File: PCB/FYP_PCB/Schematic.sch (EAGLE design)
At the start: 14 parts, among them IC1 7805TV

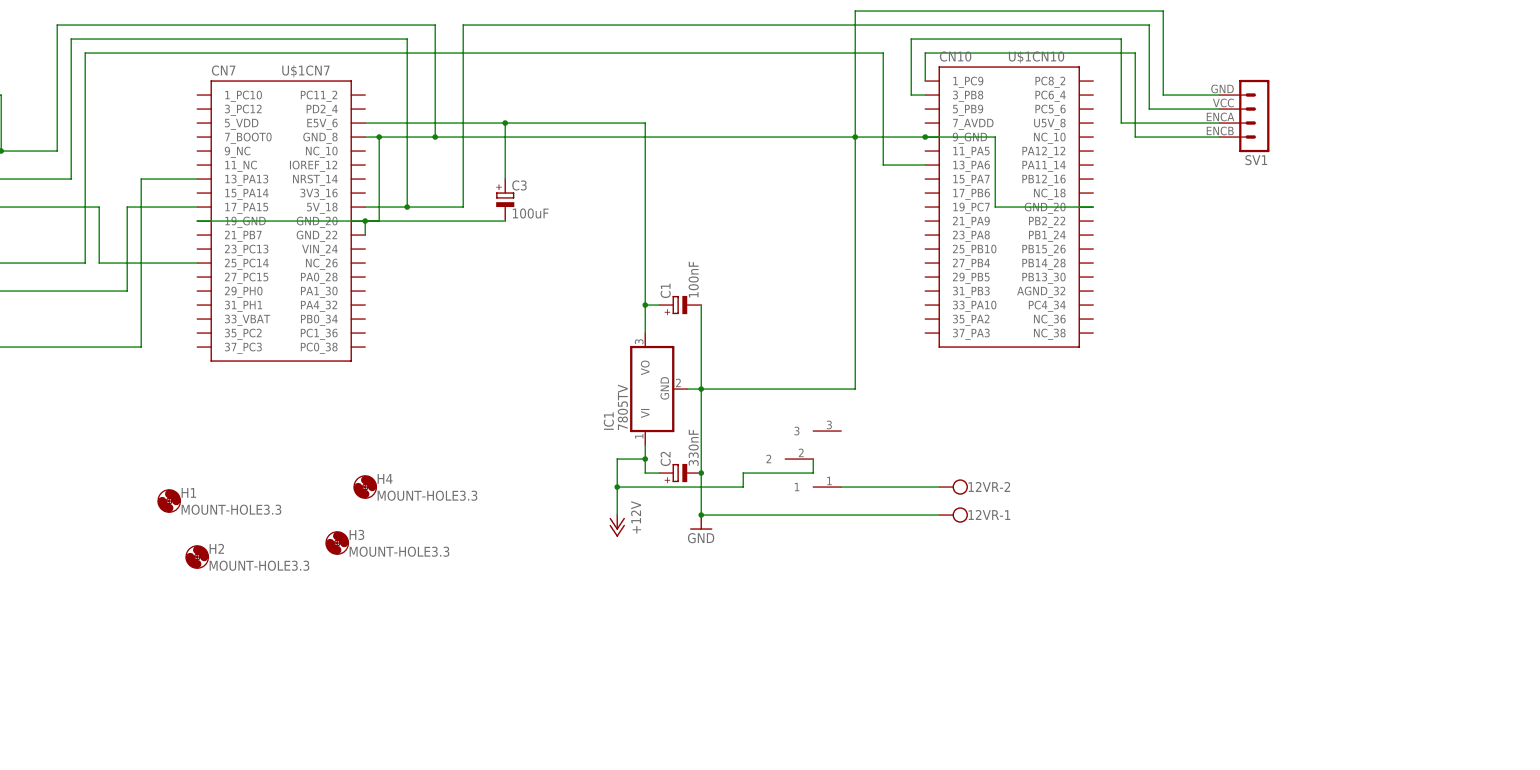
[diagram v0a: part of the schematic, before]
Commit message: Update PCB for new pin configurations. Add HC05 bluetooth module.
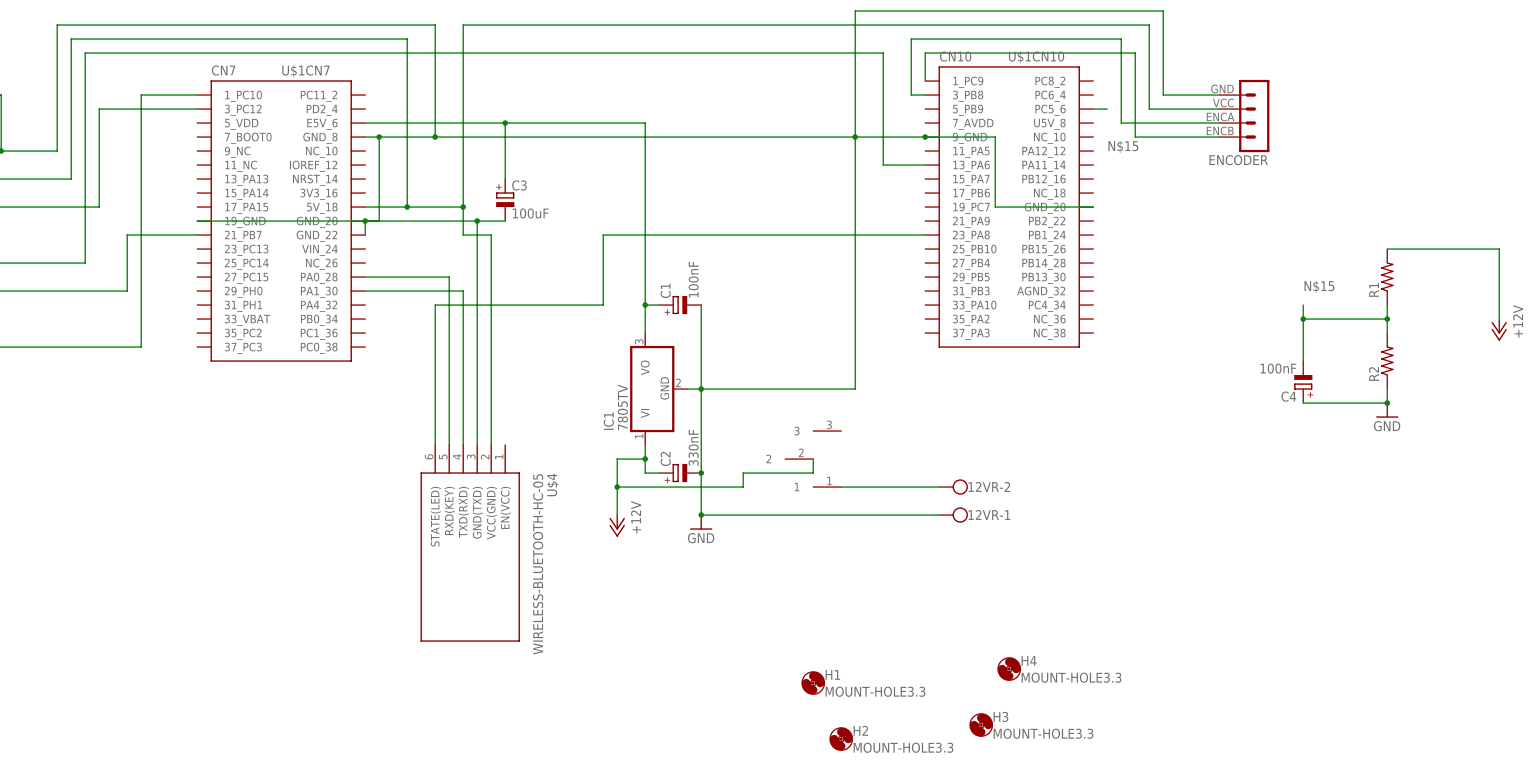
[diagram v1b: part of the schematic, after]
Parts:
- added C4: 100nF, rcl:CPOL-EUE2.5-5
- added R1, R2: (no value), rcl:R-US_0204/7
- added U$4: WIRELESS-BLUETOOTH-HC-05, BT_6pin:WIRELESS-BLUETOOTH-HC-05
- renumbered SV1 to ENCODER
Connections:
- new net N$11: U$1CN7.PA0_28, U$4.RXD(KEY)
- new net N$12: U$1CN10.23_PA8, U$4.STATE(LED)
- new net N$15: C4.-, R1.1, R2.2, U$1CN10.PC5_6
- new net N$9: U$1CN7.PA1_30, U$4.TXD(RXD)
- net +12V: now also R1.2
- net GND: now also C4.+, R2.1, U$4.GND(TXD)
- net N$1: now also U$1CN7.1_PC10; no longer U$1CN7.13_PA13
- net N$2: now also U$1CN7.21_PB7; no longer U$1CN7.17_PA15
- net N$4: now also U$1CN7.3_PC12; no longer U$1CN7.25_PC14
- net N$5: now also U$4.VCC(GND)
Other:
- moved on the sheet: H1, H2, H3, H4

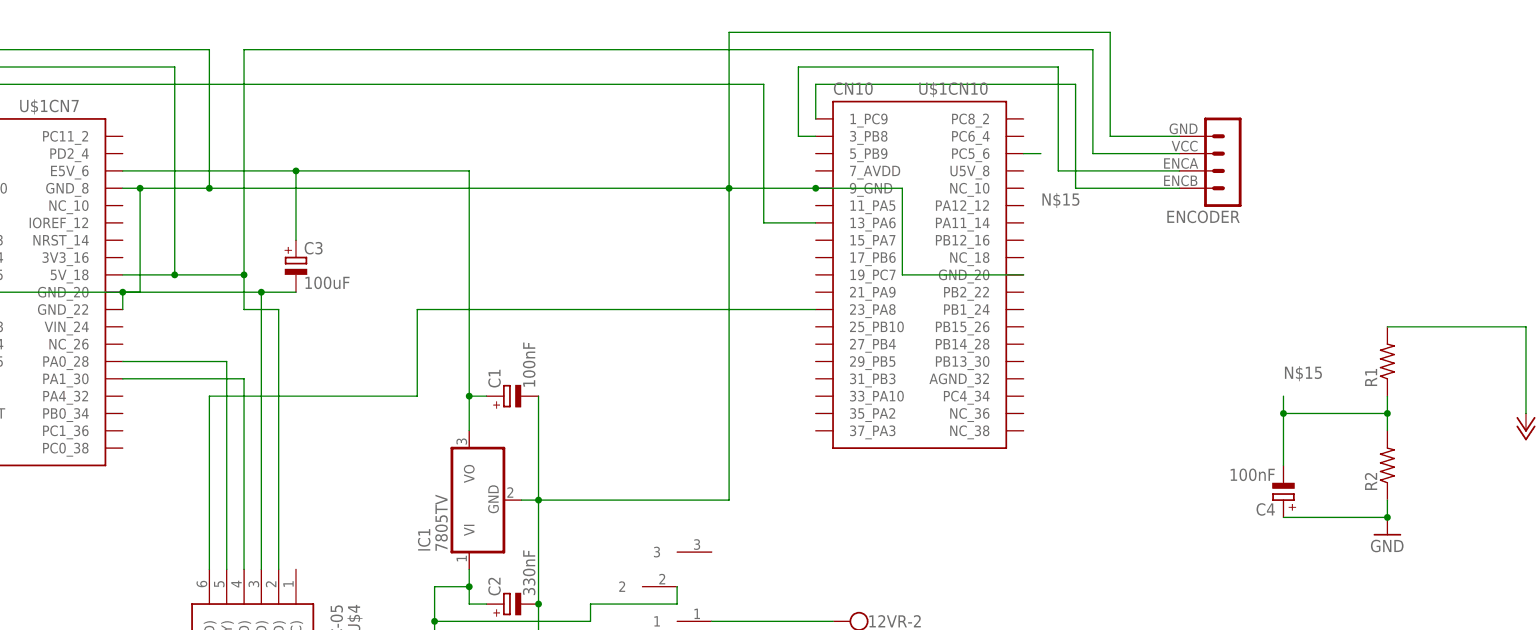
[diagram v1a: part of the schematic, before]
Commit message: Eagle garbage I cant gitignore.
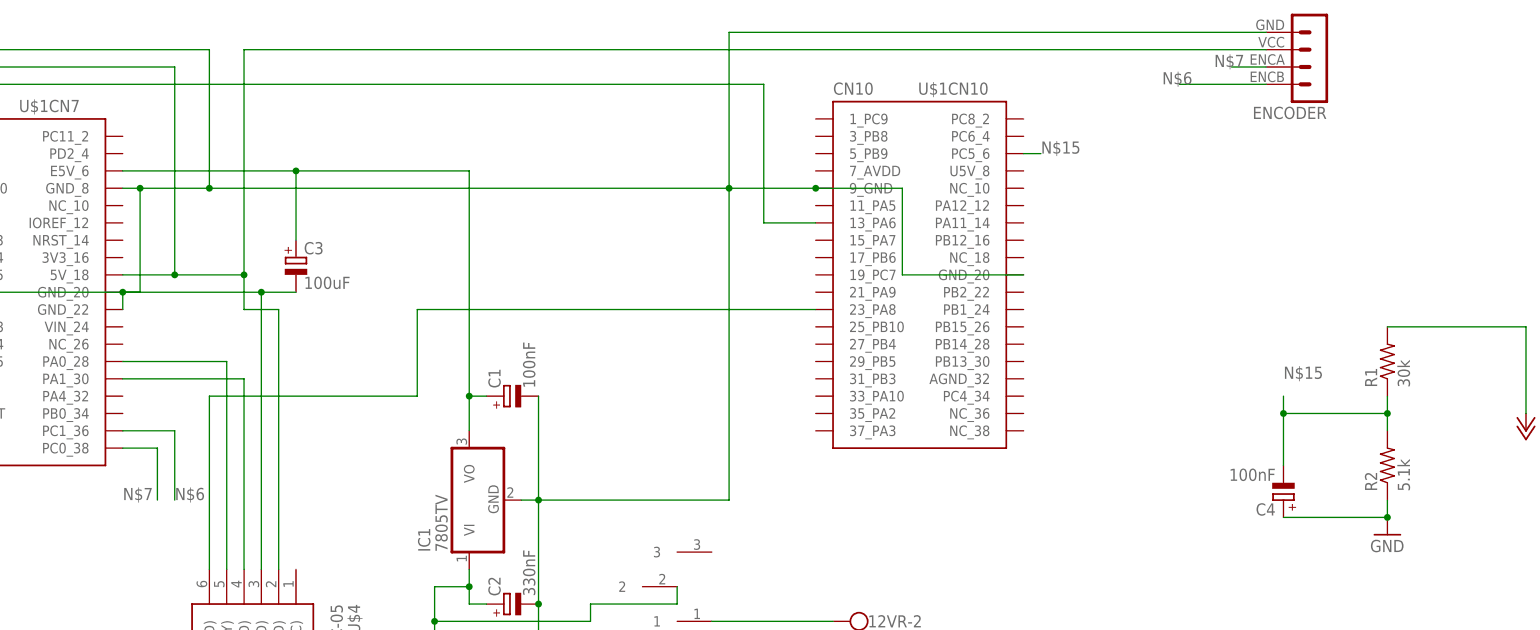
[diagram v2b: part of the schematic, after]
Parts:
- R1: value (none) -> 30k
- R2: value (none) -> 5.1k
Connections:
- net N$6: now also U$1CN7.PC1_36; no longer U$1CN10.1_PC9
- net N$7: now also U$1CN7.PC0_38; no longer U$1CN10.3_PB8
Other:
- moved on the sheet: ENCODER
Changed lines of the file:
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@@
 <part name="U$3" library="Custom" deviceset="TOGGLESWITCH" device=""/>
 <part name="U$4" library="BT_6pin" deviceset="WIRELESS-BLUETOOTH-HC-05" device=""/>
-<part name="R1" library="rcl" library_urn="urn:adsk.eagle:library:334" deviceset="R-US_" device="0204/7" package3d_urn="urn:adsk.eagle:package:23498/2"/>
-<part name="R2" library="rcl" library_urn="urn:adsk.eagle:library:334" deviceset="R-US_" device="0204/7" package3d_urn="urn:adsk.eagle:package:23498/2"/>
+<part name="R1" library="rcl" library_urn="urn:adsk.eagle:library:334" deviceset="R-US_" device="0204/7" package3d_urn="urn:adsk.eagle:package:23498/2" value="30k"/>
+<part name="R2" library="rcl" library_urn="urn:adsk.eagle:library:334" deviceset="R-US_" device="0204/7" package3d_urn="urn:adsk.eagle:package:23498/2" value="5.1k"/>
 <part name="P+3" library="supply1" library_urn="urn:adsk.eagle:library:371" deviceset="+12V" device=""/>
 <part name="GND3" library="supply1" library_urn="urn:adsk.eagle:library:371" deviceset="GND" device=""/>
@@
 <attribute name="VALUE" x="76.2" y="-15.24" size="1.778" layer="96"/>
 </instance>
-<instance part="ENCODER" gate="1" x="180.34" y="60.96" smashed="yes" rot="R180">
-<attribute name="VALUE" x="181.61" y="71.12" size="1.778" layer="96" rot="R180"/>
-<attribute name="NAME" x="181.61" y="55.118" size="1.778" layer="95" rot="R180"/>
+<instance part="ENCODER" gate="1" x="193.04" y="76.2" smashed="yes" rot="R180">
+<attribute name="VALUE" x="194.31" y="86.36" size="1.778" layer="96" rot="R180"/>
+<attribute name="NAME" x="194.31" y="70.358" size="1.778" layer="95" rot="R180"/>
 </instance>
 <instance part="P+2" gate="1" x="-142.24" y="53.34" smashed="yes" rot="R90">
@@
 <pinref part="U$1" gate="CN7" pin="5V_18"/>
 <wire x1="25.4" y1="45.72" x2="17.78" y2="45.72" width="0.1524" layer="91"/>
-<pinref part="ENCODER" gate="1" pin="2"/>
-<wire x1="172.72" y1="63.5" x2="160.02" y2="63.5" width="0.1524" layer="91"/>
-<wire x1="160.02" y1="63.5" x2="160.02" y2="78.74" width="0.1524" layer="91"/>
-<wire x1="160.02" y1="78.74" x2="35.56" y2="78.74" width="0.1524" layer="91"/>
+<wire x1="185.42" y1="78.74" x2="35.56" y2="78.74" width="0.1524" layer="91"/>
 <wire x1="35.56" y1="78.74" x2="35.56" y2="45.72" width="0.1524" layer="91"/>
 <wire x1="35.56" y1="45.72" x2="25.4" y2="45.72" width="0.1524" layer="91"/>
@@
 <wire x1="35.56" y1="40.64" x2="35.56" y2="45.72" width="0.1524" layer="91"/>
 <junction x="35.56" y="45.72"/>
+<pinref part="ENCODER" gate="1" pin="2"/>
 </segment>
 </net>
@@
 <wire x1="30.48" y1="58.42" x2="106.68" y2="58.42" width="0.1524" layer="91"/>
 <junction x="30.48" y="58.42"/>
-<pinref part="ENCODER" gate="1" pin="1"/>
 <wire x1="106.68" y1="58.42" x2="119.38" y2="58.42" width="0.1524" layer="91"/>
-<wire x1="172.72" y1="66.04" x2="162.56" y2="66.04" width="0.1524" layer="91"/>
-<wire x1="162.56" y1="66.04" x2="162.56" y2="81.28" width="0.1524" layer="91"/>
-<wire x1="162.56" y1="81.28" x2="106.68" y2="81.28" width="0.1524" layer="91"/>
+<wire x1="185.42" y1="81.28" x2="106.68" y2="81.28" width="0.1524" layer="91"/>
 <wire x1="106.68" y1="81.28" x2="106.68" y2="58.42" width="0.1524" layer="91"/>
 <junction x="106.68" y="58.42"/>
@@
 <wire x1="38.1" y1="2.54" x2="38.1" y2="43.18" width="0.1524" layer="91"/>
 <junction x="38.1" y="43.18"/>
+<pinref part="ENCODER" gate="1" pin="1"/>
 </segment>
 <segment>
@@
 </segment>
 </net>
-<net name="N$6" class="0">
-<segment>
-<pinref part="ENCODER" gate="1" pin="4"/>
-<wire x1="172.72" y1="58.42" x2="157.48" y2="58.42" width="0.1524" layer="91"/>
-<wire x1="157.48" y1="58.42" x2="157.48" y2="73.66" width="0.1524" layer="91"/>
-<wire x1="157.48" y1="73.66" x2="119.38" y2="73.66" width="0.1524" layer="91"/>
-<pinref part="U$1" gate="CN10" pin="1_PC9"/>
-<wire x1="119.38" y1="73.66" x2="119.38" y2="68.58" width="0.1524" layer="91"/>
-</segment>
-</net>
-<net name="N$7" class="0">
-<segment>
-<pinref part="ENCODER" gate="1" pin="3"/>
-<wire x1="172.72" y1="60.96" x2="154.94" y2="60.96" width="0.1524" layer="91"/>
-<wire x1="154.94" y1="60.96" x2="154.94" y2="76.2" width="0.1524" layer="91"/>
-<wire x1="154.94" y1="76.2" x2="116.84" y2="76.2" width="0.1524" layer="91"/>
-<wire x1="116.84" y1="76.2" x2="116.84" y2="66.04" width="0.1524" layer="91"/>
-<pinref part="U$1" gate="CN10" pin="3_PB8"/>
-<wire x1="116.84" y1="66.04" x2="119.38" y2="66.04" width="0.1524" layer="91"/>
-</segment>
-</net>
 <net name="N$8" class="0">
 <segment>
@@
 <pinref part="U$1" gate="CN10" pin="PC5_6"/>
 <wire x1="149.86" y1="63.5" x2="152.4" y2="63.5" width="0.1524" layer="91"/>
-<label x="152.4" y="55.88" size="1.778" layer="95"/>
+<label x="152.4" y="63.5" size="1.778" layer="95"/>
 </segment>
 <segment>
@@
 </segment>
 </net>
+<net name="N$6" class="0">
+<segment>
+<pinref part="U$1" gate="CN7" pin="PC1_36"/>
+<wire x1="17.78" y1="22.86" x2="25.4" y2="22.86" width="0.1524" layer="91"/>
+<wire x1="25.4" y1="22.86" x2="25.4" y2="12.7" width="0.1524" layer="91"/>
+<label x="25.4" y="12.7" size="1.778" layer="95"/>
+</segment>
+<segment>
+<pinref part="ENCODER" gate="1" pin="4"/>
+<wire x1="185.42" y1="73.66" x2="172.72" y2="73.66" width="0.1524" layer="91"/>
+<label x="170.18" y="73.66" size="1.778" layer="95"/>
+</segment>
+</net>
+<net name="N$7" class="0">
+<segment>
+<pinref part="U$1" gate="CN7" pin="PC0_38"/>
+<wire x1="17.78" y1="20.32" x2="22.86" y2="20.32" width="0.1524" layer="91"/>
+<wire x1="22.86" y1="20.32" x2="22.86" y2="12.7" width="0.1524" layer="91"/>
+<label x="17.78" y="12.7" size="1.778" layer="95"/>
+</segment>
+<segment>
+<pinref part="ENCODER" gate="1" pin="3"/>
+<wire x1="185.42" y1="76.2" x2="180.34" y2="76.2" width="0.1524" layer="91"/>
+<label x="177.8" y="76.2" size="1.778" layer="95"/>
+</segment>
+</net>

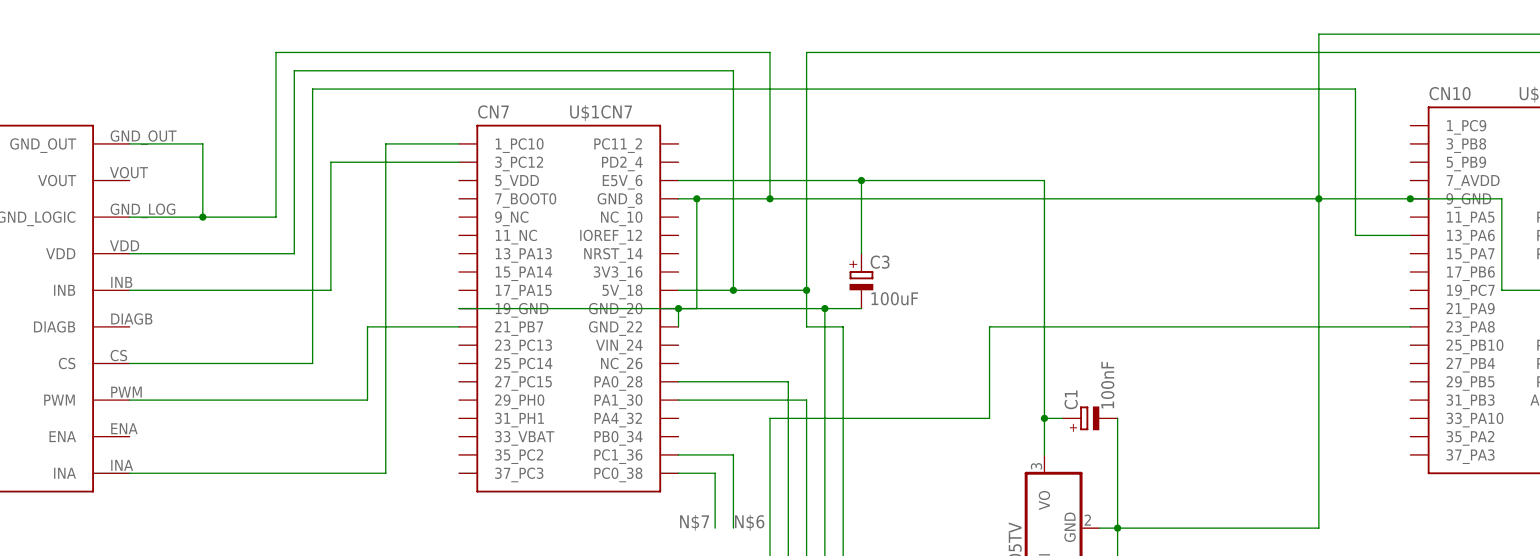
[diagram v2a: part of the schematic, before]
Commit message: Update PCB to put CS on an ADC pin.
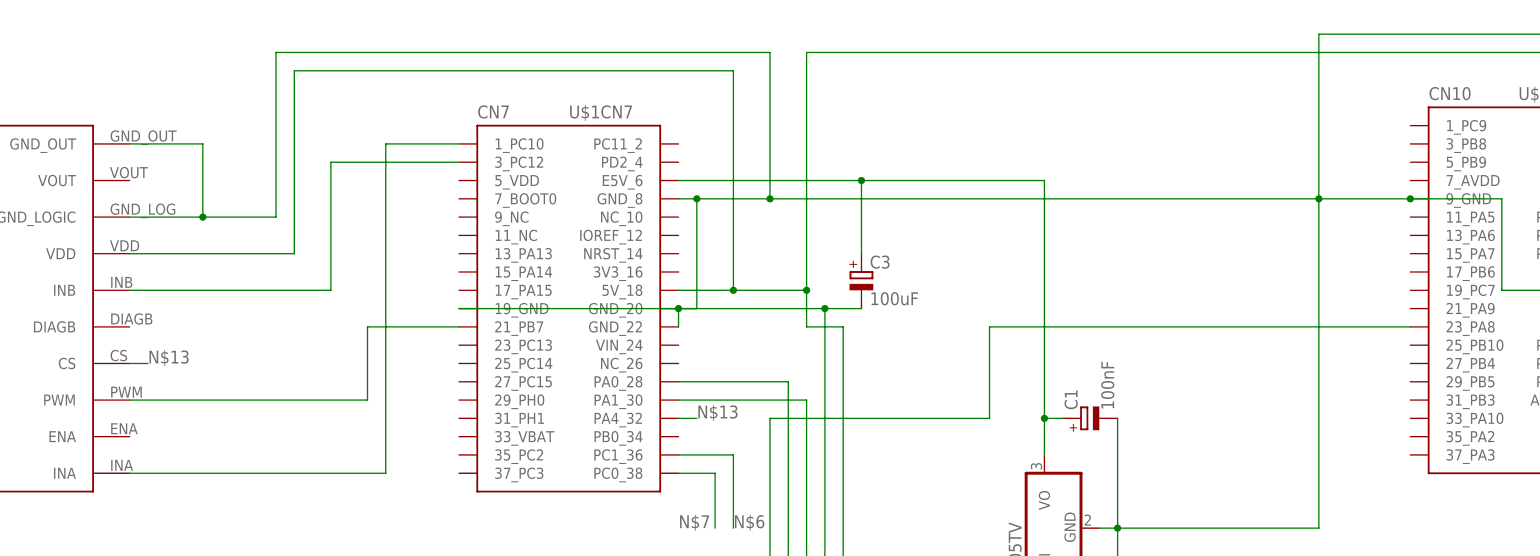
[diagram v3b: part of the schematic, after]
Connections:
- removed net N$3: U$1CN10.13_PA6, U$2.CS
- new net N$13: U$1CN7.PA4_32, U$2.CS
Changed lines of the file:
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@@
-</segment>
-</net>
-<net name="N$3" class="0">
-<segment>
-<wire x1="-33.02" y1="73.66" x2="111.76" y2="73.66" width="0.1524" layer="91"/>
-<wire x1="111.76" y1="73.66" x2="111.76" y2="53.34" width="0.1524" layer="91"/>
-<pinref part="U$1" gate="CN10" pin="13_PA6"/>
-<wire x1="-33.02" y1="73.66" x2="-33.02" y2="35.56" width="0.1524" layer="91"/>
-<pinref part="U$2" gate="G$1" pin="CS"/>
-<wire x1="-33.02" y1="35.56" x2="-58.42" y2="35.56" width="0.1524" layer="91"/>
-<wire x1="119.38" y1="53.34" x2="111.76" y2="53.34" width="0.1524" layer="91"/>
 </segment>
 </net>
@@
 </segment>
 </net>
+<net name="N$13" class="0">
+<segment>
+<pinref part="U$2" gate="G$1" pin="CS"/>
+<wire x1="-58.42" y1="35.56" x2="-55.88" y2="35.56" width="0.1524" layer="91"/>
+<label x="-55.88" y="35.56" size="1.778" layer="95"/>
+</segment>
+<segment>
+<pinref part="U$1" gate="CN7" pin="PA4_32"/>
+<wire x1="17.78" y1="27.94" x2="20.32" y2="27.94" width="0.1524" layer="91"/>
+<label x="20.32" y="27.94" size="1.778" layer="95"/>
+</segment>
+</net>

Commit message: Change PCB layout and generate gerber files for production.
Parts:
- removed ENCODER: (no value), Custom:MA04-1
- added SV1: (no value), Custom:MA06-1
- added X2: (no value), con-wago-500:W237-102
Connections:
- new net N$14: SV1.MTRPWR, X2-2.KL
- new net N$3: SV1.MTRPWR-, X2-1.KL
- net GND: now also SV1.ENCGND; no longer ENCODER.1
- net N$5: now also SV1.ENCVCC; no longer ENCODER.2
- net N$6: now also SV1.ENCA; no longer ENCODER.4
- net N$7: now also SV1.ENCB; no longer ENCODER.3
